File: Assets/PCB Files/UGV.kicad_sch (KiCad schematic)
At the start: 76 parts, among them J13 USB3_A, J15 Screw_Terminal_01x12, J16 Screw_Terminal_01x12, J17 Screw_Terminal_01x12, J18 Screw_Terminal_01x12, U1 INA219AxDCN, U2 LMR33630ADDA, U3 SN74LVC8T245, U4 Teensy4.1, U5 SN74LVC8T245

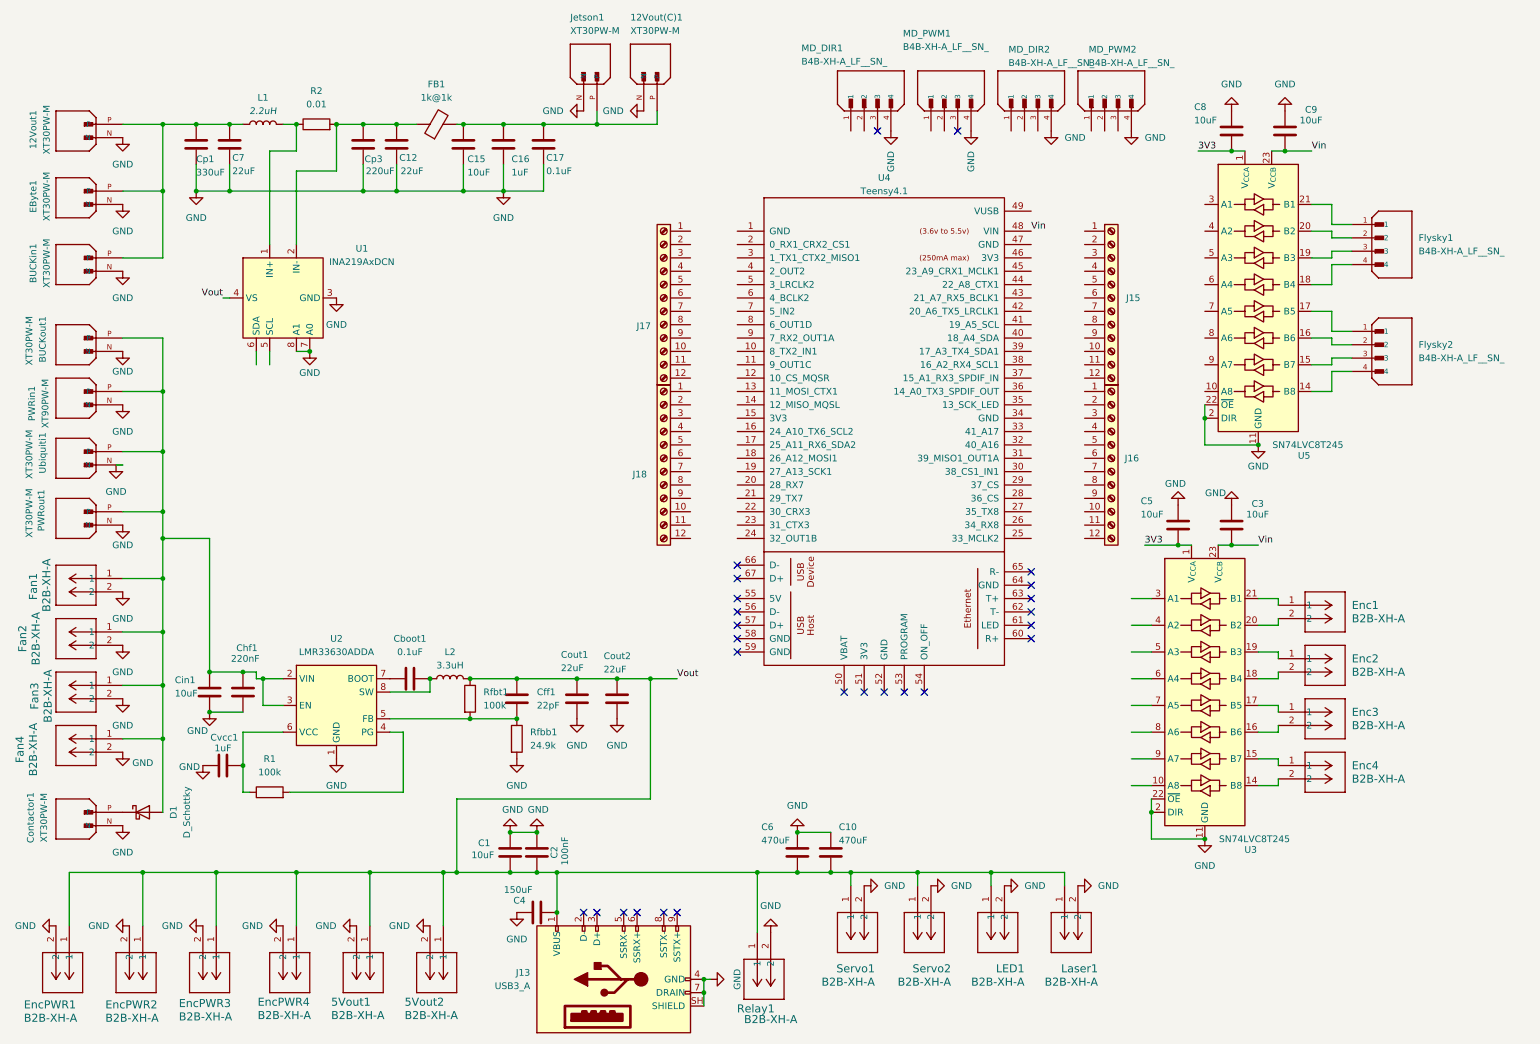
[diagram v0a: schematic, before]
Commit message: Added Logo and edited layout
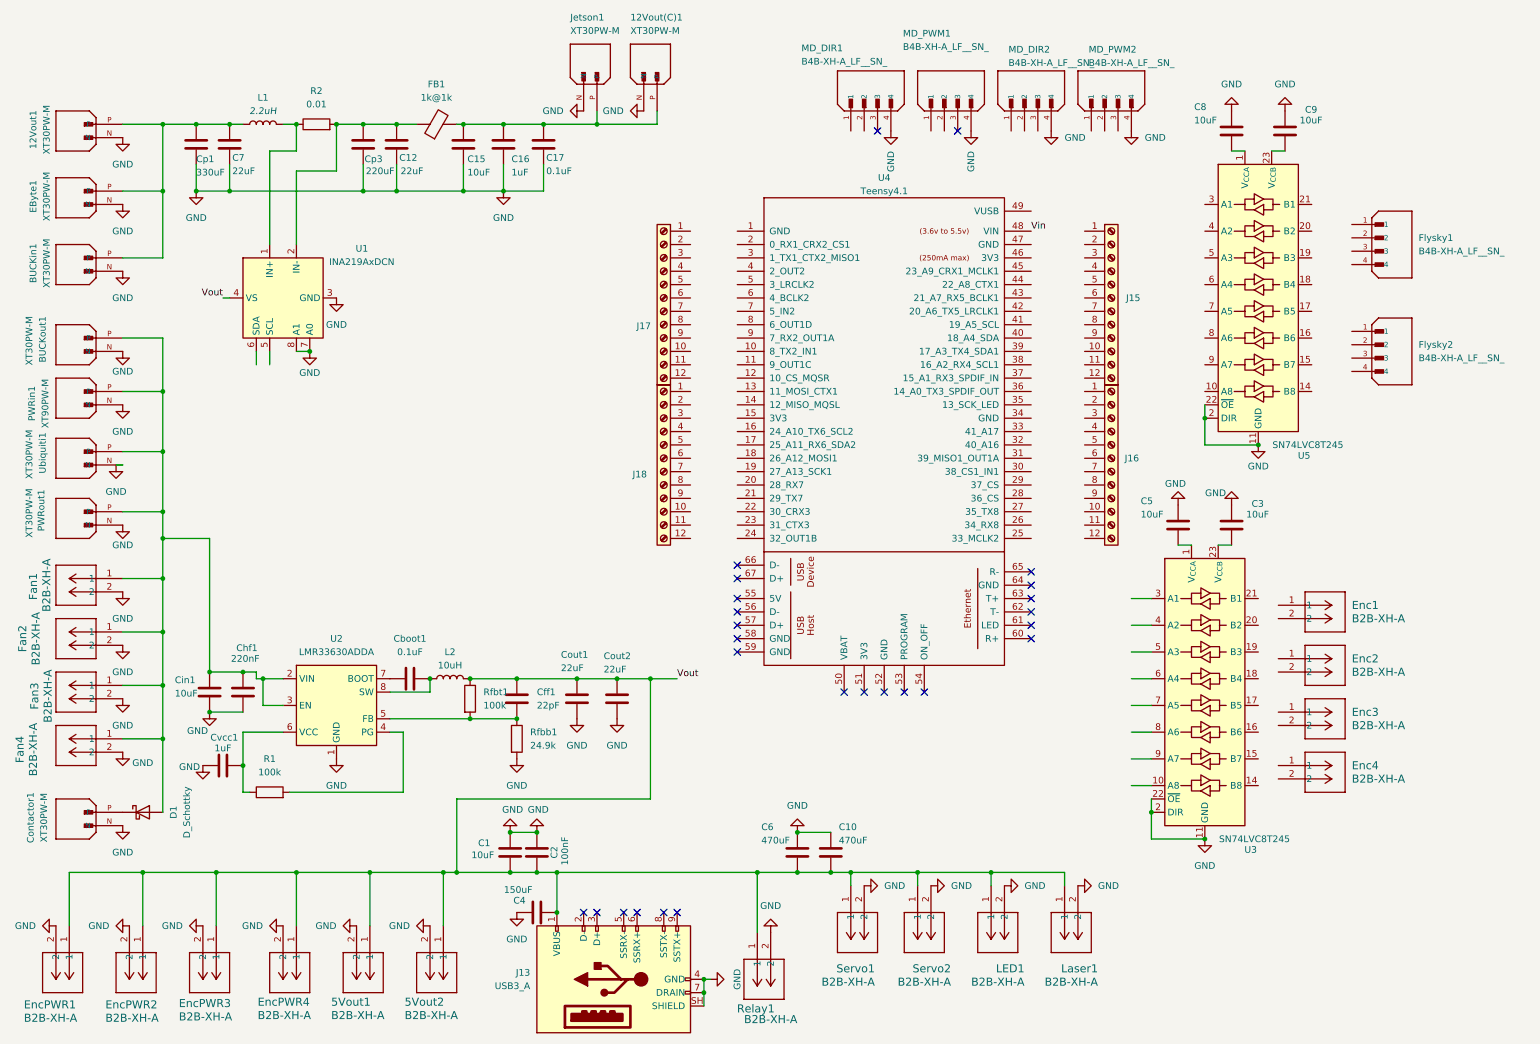
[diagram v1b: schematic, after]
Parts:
- L2: value 3.3uH -> 10uH
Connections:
- net Vin: no longer C3.2, C9.2, U3.23 (V_{CCB}), U3.24 (V_{CCB}), U5.23 (V_{CCB}), U5.24 (V_{CCB})
- net at U5.14 (B8): no longer Flysky2.4
- net at U5.15 (B7): no longer Flysky2.3
- net at U5.16 (B6): no longer Flysky2.2
- net at U5.17 (B5): no longer Flysky2.1
- net at U5.18 (B4): no longer Flysky1.4
- net at U5.19 (B3): no longer Flysky1.3
- net at U5.20 (B2): no longer Flysky1.2
- net at U5.21 (B1): no longer Flysky1.1
- net at U3.14 (B8): no longer Enc4.2
- net at U3.15 (B7): no longer Enc4.1
- net at U3.16 (B6): no longer Enc3.2
- net at U3.17 (B5): no longer Enc3.1
- net at U3.18 (B4): no longer Enc2.2
- net at U3.19 (B3): no longer Enc2.1
- net at U3.20 (B2): no longer Enc1.2
- net at U3.21 (B1): no longer Enc1.1
- net 3V3: no longer names the net of C8.2, U5.1 (V_{CCA})
- net 3V3: no longer C5.2, U3.1 (V_{CCA})
- new net: C9.2, U5.23 (V_{CCB}), U5.24 (V_{CCB})
- new net: C5.2, U3.1 (V_{CCA})
- new net: C3.2, U3.23 (V_{CCB}), U3.24 (V_{CCB})
